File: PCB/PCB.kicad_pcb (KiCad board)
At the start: 2 copper layers, 184.2 x 71.2 mm, 92 parts, among them J1 Conn_01x02, J2 Conn_01x02, U1 ADXL345, U2 Seeed Studio XIAO nRF52840, U3 ADXL345, U4 Seeed Studio XIAO nRF52840

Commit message: bulk
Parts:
- moved R3 2.15 mm to (206.5, 47.1)
- moved R4 1.70 mm to (206.5, 49.0)
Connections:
- R1 pad 1: /SCL -> +3.3V
- R1 pad 2: Net-(U2-P0.05_A5_D5_SCL) -> /SCL
- R2 pad 1: /SDA -> +3.3V
- R2 pad 2: Net-(U2-P0.04_A4_D4_SDA) -> /SDA
- R3 pad 1: /SDAB -> +3.3VA
- R3 pad 2: Net-(U4-P0.04_A4_D4_SDA) -> /SCLB
- R4 pad 1: /SCLB -> +3.3VA
- R4 pad 2: Net-(U4-P0.05_A5_D5_SCL) -> /SDAB
- U1 pad 12: unconnected-(U1-SDO/ALT_ADDRESS-Pad12) -> GND
- U1 pad 7: GND -> +3.3V
- U2 pad 5: Net-(U2-P0.04_A4_D4_SDA) -> /SDA
- U2 pad 6: Net-(U2-P0.05_A5_D5_SCL) -> /SCL
- U3 pad 12: unconnected-(U3-SDO/ALT_ADDRESS-Pad12) -> GND1
- U3 pad 7: GND1 -> +3.3VA
- U4 pad 5: Net-(U4-P0.04_A4_D4_SDA) -> /SDAB
- U4 pad 6: Net-(U4-P0.05_A5_D5_SCL) -> /SCLB
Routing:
- net +3.3VA: track 21.1 -> 46.1 mm
- net /Col2: track 101.2 -> 115.5 mm
- net /Bat+: track 20.6 -> 7.28 mm
- net Net-(U4-P0.04_A4_D4_SDA): track 13.3 -> 0.00 mm
- net /SCL: track 9.42 -> 19.4 mm
- net +3.3V: track 46.5 -> 55.0 mm, vias 2 -> 4
- net Net-(U4-P0.05_A5_D5_SCL): track 8.35 -> 0.00 mm
- net /SDAB: track 37.0 -> 41.4 mm
- net /SDA: track 5.79 -> 10.0 mm
- net /SCLB: track 34.8 -> 38.8 mm, vias 2 -> 4
- net Net-(U2-P0.05_A5_D5_SCL): track 2.60 -> 0.00 mm
- net Net-(U2-P0.04_A4_D4_SDA): track 2.60 -> 0.00 mm
- net /Bat-B: track 28.7 -> 29.9 mm
- net GND: track 40.3 -> 39.2 mm
- net /Bat+B: track 32.9 -> 34.0 mm
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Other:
- outline, holes or cut-outs redrawn
- board text added: "Board: 2Pocket Version: 1.1 Developer: Parks Date: 08/24/24"

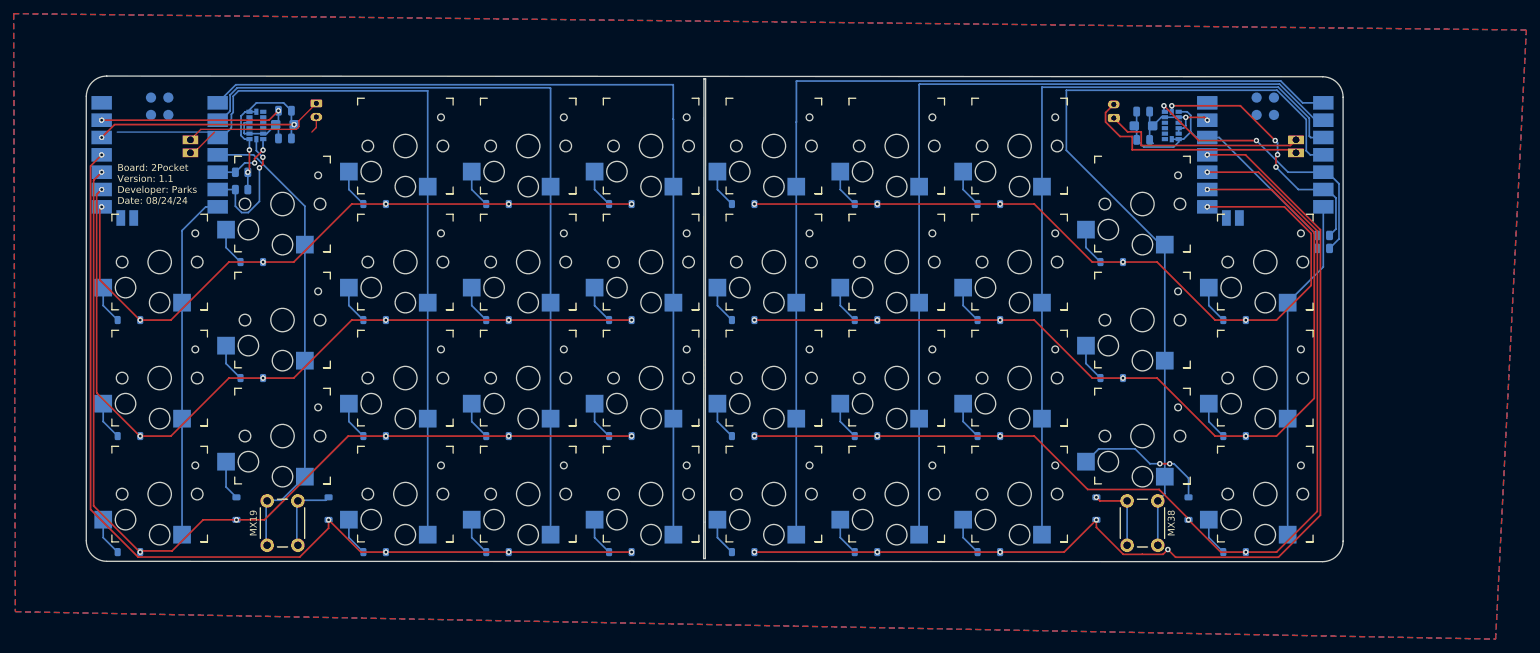
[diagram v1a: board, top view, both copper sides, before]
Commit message: 1.2 changes for pass through charging and mounting
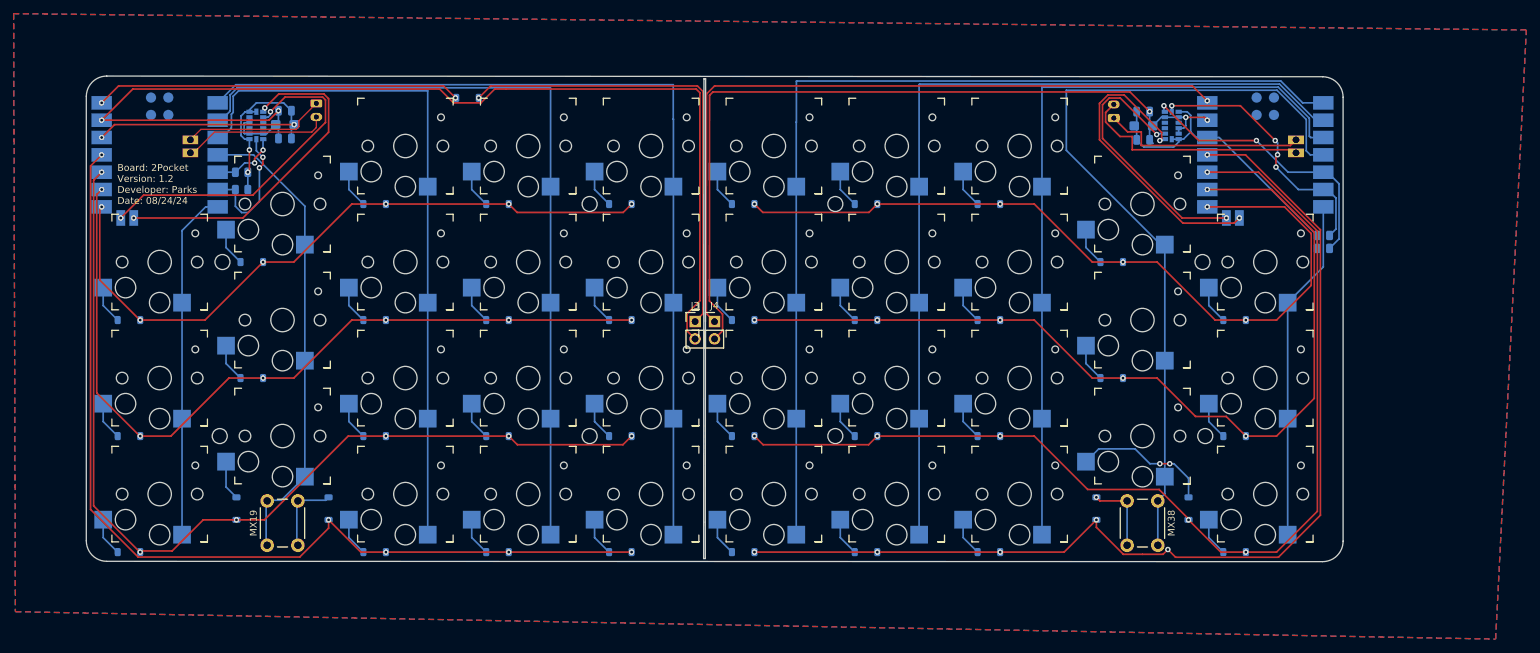
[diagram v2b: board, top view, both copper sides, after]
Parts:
- added D39: D_Schottky, Diode_SMD:D_SOD-123, B.Cu at (81.1, 26.9)
- added J3: Conn_01x02, Connector_PinHeader_2.54mm:PinHeader_1x02_P2.54mm_Vertical, F.Cu at (114.5, 59.7)
- added J4: Conn_01x02, Connector_PinHeader_2.54mm:PinHeader_1x02_P2.54mm_Vertical, F.Cu at (117.3, 59.7)
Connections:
- U1 pad 8: unconnected-(U1-INT1-Pad8) -> /I1
- U1 pad 9: unconnected-(U1-INT2-Pad9) -> /I2
- U2 pad 14: unconnected-(U2-5V-Pad14) -> +5V
- U2 pad 19: unconnected-(U2-P0.09_NFC1-Pad19) -> /I1
- U2 pad 20: unconnected-(U2-P0.10_NFC2-Pad20) -> /I2
- U3 pad 8: unconnected-(U3-INT1-Pad8) -> /I1B
- U3 pad 9: unconnected-(U3-INT2-Pad9) -> /I2B
- U4 pad 14: unconnected-(U4-5V-Pad14) -> +5VA
- U4 pad 19: unconnected-(U4-P0.09_NFC1-Pad19) -> /I1B
- U4 pad 20: unconnected-(U4-P0.10_NFC2-Pad20) -> /I2B
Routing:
- net GND: track 39.2 -> 168.0 mm
- net +5VA: track 0.00 -> 108.6 mm, vias 0 -> 1
- net GND1: track 17.2 -> 120.0 mm, vias 2 -> 3
- net Net-(D39-K): track 0.00 -> 68.1 mm, vias 0 -> 1
- net +5V: track 0.00 -> 53.7 mm, vias 0 -> 2
- net /I2: track 0.00 -> 49.9 mm, vias 0 -> 2
- net /I1: track 0.00 -> 49.8 mm, vias 0 -> 2
- net /I1B: track 0.00 -> 45.2 mm, vias 0 -> 2
- net /I2B: track 0.00 -> 39.7 mm, vias 0 -> 2
- net /Col2: track 115.5 -> 101.2 mm
- net /Bat+: track 7.28 -> 21.5 mm
- net /Row2B: track 152.8 -> 153.9 mm
- net /Row2: track 138.1 -> 139.1 mm
- net /Row0: track 98.2 -> 99.2 mm
- net /Row0B: track 115.2 -> 116.2 mm
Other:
- outline, holes or cut-outs redrawn
- board text added: "Board: 2Pocket Version: 1.2 Developer: Parks Date: 08/24/24"
- board text removed: "Board: 2Pocket Version: 1.1 Developer: Parks Date: 08/24/24"
